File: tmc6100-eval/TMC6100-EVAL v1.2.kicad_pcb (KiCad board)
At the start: 4 copper layers, 55 x 85 mm, 78 parts, among them IC301 TMC6100-LA, J201 W+P_46-3492-44-3-00-10-PPTR, Q301 BSC026N08NS5, Q302 BSC026N08NS5, Q303 BSC026N08NS5, Q304 BSC026N08NS5, Q305 BSC026N08NS5, Q306 BSC026N08NS5, U201 Metz_31330102, U203 Metz_31330103, U301 AD8418, U303 AD8418, U401 LP2985-3.3, U402 AT25128B-SSHL-T8S1-L

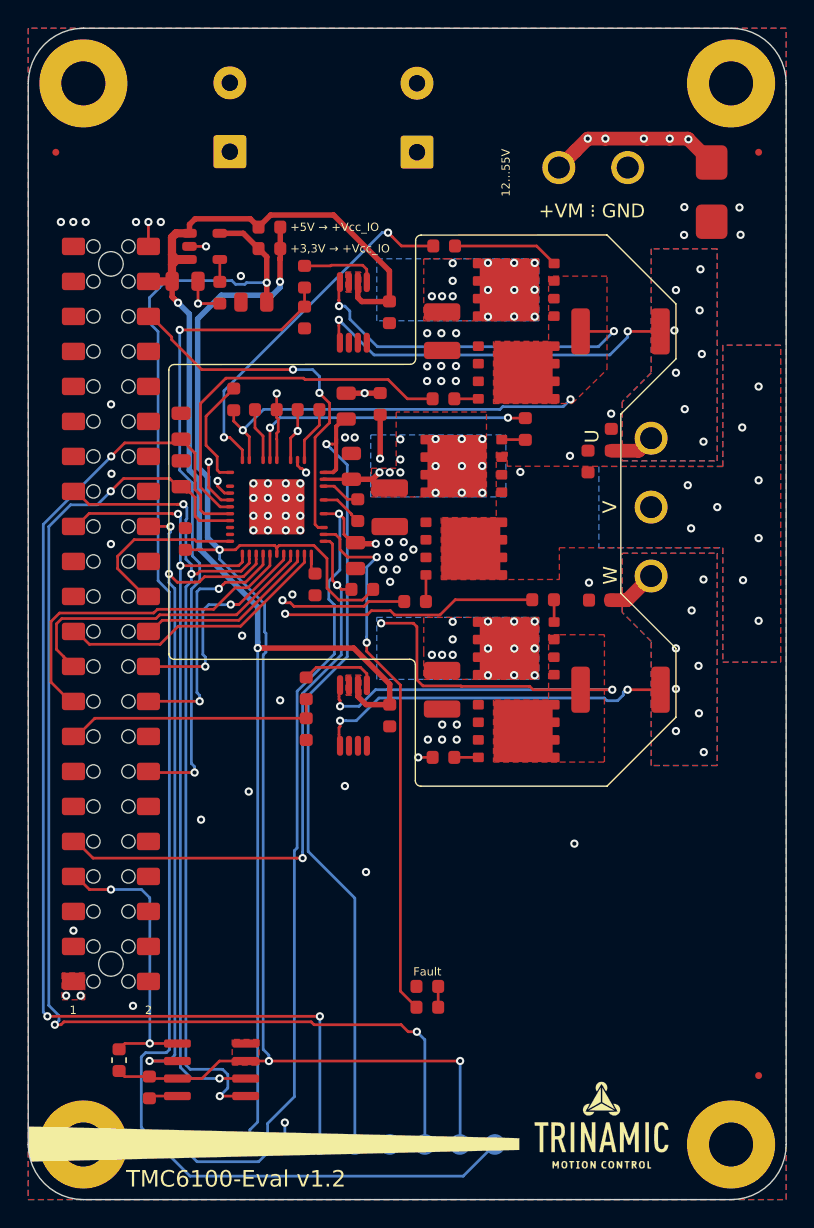
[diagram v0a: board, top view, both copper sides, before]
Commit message: upgrade to kicad6
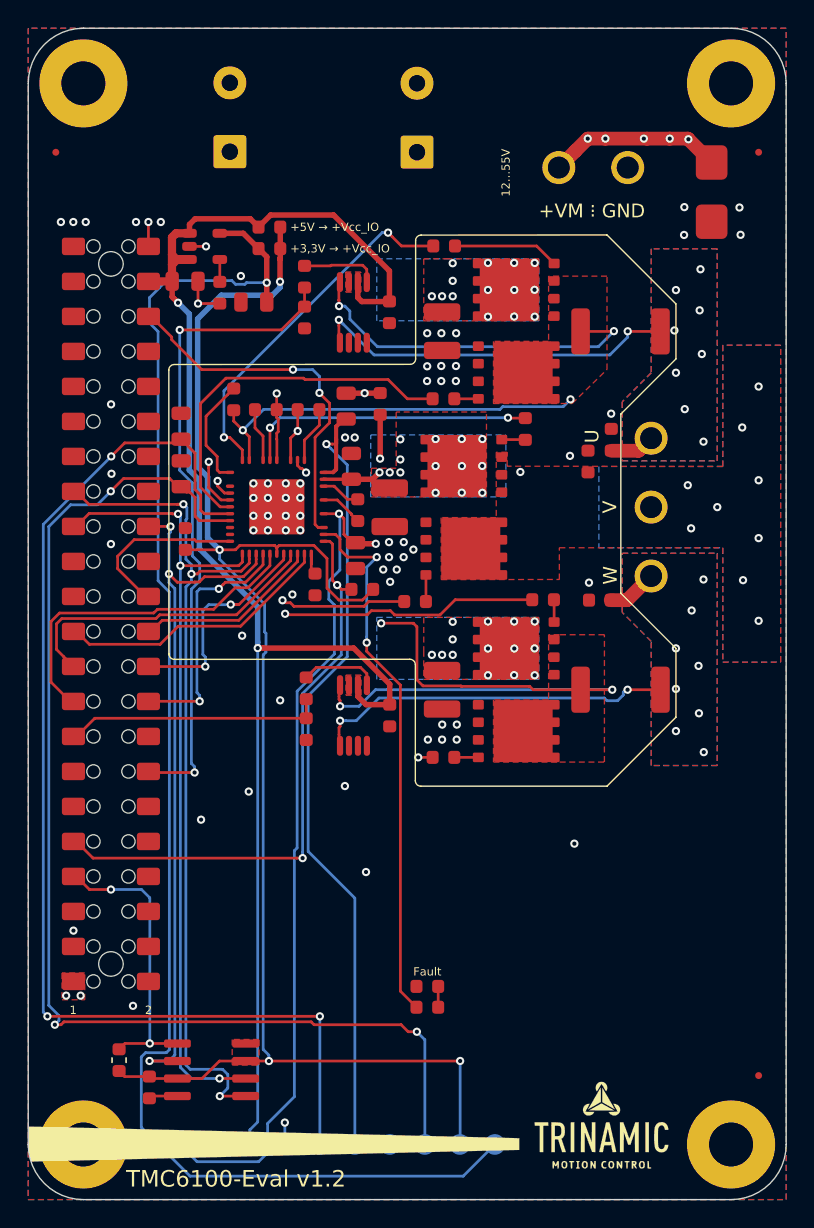
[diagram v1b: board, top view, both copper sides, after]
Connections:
- net /~CS_DRIVER renamed /~{CS_DRIVER}
- net /~CS_EEPROM renamed /~{CS_EEPROM}
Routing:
- added copper zone on In2.Cu, net /+VM
- added copper zone on In1.Cu, net GND
- removed copper zone on In3.Cu, net /+VM
- removed copper zone on In2.Cu, net GND
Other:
- net class Default removed
- net class vm removed
